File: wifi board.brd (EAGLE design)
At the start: 100 x 80 mm, 28 parts

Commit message: began routing
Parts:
- removed TRANS: RN1906FE, CUSTOM:SOT-563
- removed U$2: CH340G, CUSTOM:SOP-16
- removed U$3: BUTTON, CUSTOM:BUTTON
- removed U$4: TB6593FNG, CUSTOM:SSOP-20
- added C9: 10uF, Seeed-OPL-Capacitor:C0603
- added DRIVER: TB6593FNG, CUSTOM:SSOP-20
- added KEY: PTS645, CUSTOM:BUTTON
- added R10, R9: 10k, resistor:R0603
- added SW: RN1906FE, CUSTOM:SOT-563
- added UART: CH340G, CUSTOM:20-16
- L1: value 10uH -> DFE252012C; device Seeed-OPL-Inductor:L0603 -> CUSTOM:1008
- MDL1: device ESP8266-ESP12E:ESP8266-ESP12E -> adafruit:ESP-12
- R7: value 330k -> 285
- moved C8 225.8 mm to (61.0, 12.1), turned to 180 degrees
- moved U1 221.0 mm to (76.2, 2.54), turned to 90 degrees
- moved D1 219.8 mm to (69.2, 3.81), turned to 90 degrees
- moved C7 216.0 mm to (74.9, 16.5)
- moved R6 214.1 mm to (69.8, 11.4)
- moved R2 211.4 mm to (70.5, 8.89)
- moved C6 207.1 mm to (66.7, 23.5), turned to 90 degrees
- moved R8 206.1 mm to (35.6, 21.0), turned to 270 degrees
- moved R7 201.6 mm to (33.7, 21.0), turned to 90 degrees
- moved C5 198.0 mm to (66.7, 13.3), turned to 90 degrees
- moved CLK 195.7 mm to (67.9, 18.4), turned to 90 degrees
- moved R1 176.1 mm to (51.4, 33.0)
- moved C4 163.9 mm to (59.1, 12.1), turned to 180 degrees
- moved C2 134.6 mm to (35.6, 15.2)
- moved L1 133.7 mm to (34.9, 12.1), turned to 180 degrees
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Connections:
- removed net N$8: OPAMP.4, R7.2
- removed net SLP: REG.8
- new net GP14: MDL1.5
- new net GP15: MDL1.10, R9.2
- new net GP16: MDL1.4
- new net GP2: MDL1.11, R10.2
- new net IN1: DRIVER.18, MDL1.7
- new net IN2: DRIVER.19, MDL1.6
- new net M1: DRIVER.6, DRIVER.7
- new net M2: DRIVER.14, DRIVER.15
- new net PWM: DRIVER.2, MDL1.14
- new net STBY: DRIVER.3, MDL1.13
- net +3V3: now also C9.2, DRIVER.20, L1.P$3, R10.1, REG.8, UART.16, UART.4; no longer L1.2, U$2.16, U$2.4
- net ADC: now also OPAMP.4, R7.2
- net D+: now also UART.5; no longer U$2.5
- net D-: now also UART.6; no longer U$2.6
- net DTR: now also SW.1, SW.5, UART.13; no longer TRANS.1, TRANS.5, U$2.13
- net GND: now also C9.1, DRIVER.1, DRIVER.10, DRIVER.11, DRIVER.12, DRIVER.13, DRIVER.8, DRIVER.9, KEY.3, R9.1, UART.1; no longer U$2.1, U$3.3
- net GP0: now also SW.6; no longer TRANS.6
- net N$1: now also UART.2; no longer U$2.2
- net N$4: now also L1.P$2; no longer L1.1
- net N$7: now also UART.3; no longer U$2.3
- net RST: now also KEY.1, SW.3; no longer TRANS.3
- net RTS: now also SW.2, SW.4, UART.14; no longer TRANS.2, TRANS.4, U$2.14
- net VCC: now also DRIVER.16, DRIVER.17, DRIVER.4, DRIVER.5
- net XI: now also UART.7; no longer U$2.7
- net XO: now also UART.8; no longer U$2.8
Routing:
- net +3V3: track 0.00 -> 100.5 mm, vias 0 -> 7
- net STBY: track 0.00 -> 52.9 mm, vias 0 -> 2
- net PWM: track 0.00 -> 50.3 mm, vias 0 -> 2
- net TX: track 0.00 -> 44.8 mm, vias 0 -> 2
- net VCC: track 0.00 -> 44.4 mm
- net RX: track 0.00 -> 39.7 mm, vias 0 -> 2
- net N$15: track 0.00 -> 29.8 mm, vias 0 -> 2
- net ADC: track 0.00 -> 25.2 mm
- net IN1: track 0.00 -> 18.4 mm
- net N$5: track 0.00 -> 17.2 mm, vias 0 -> 2
- net IN2: track 0.00 -> 15.8 mm
- net N$16: track 0.00 -> 14.9 mm
- net N$17: track 0.00 -> 14.8 mm
- net D-: track 0.00 -> 9.06 mm, vias 0 -> 2
- net N$3: track 0.00 -> 8.67 mm
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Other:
- board size 100 x 80 mm -> 71.1 x 35.6 mm

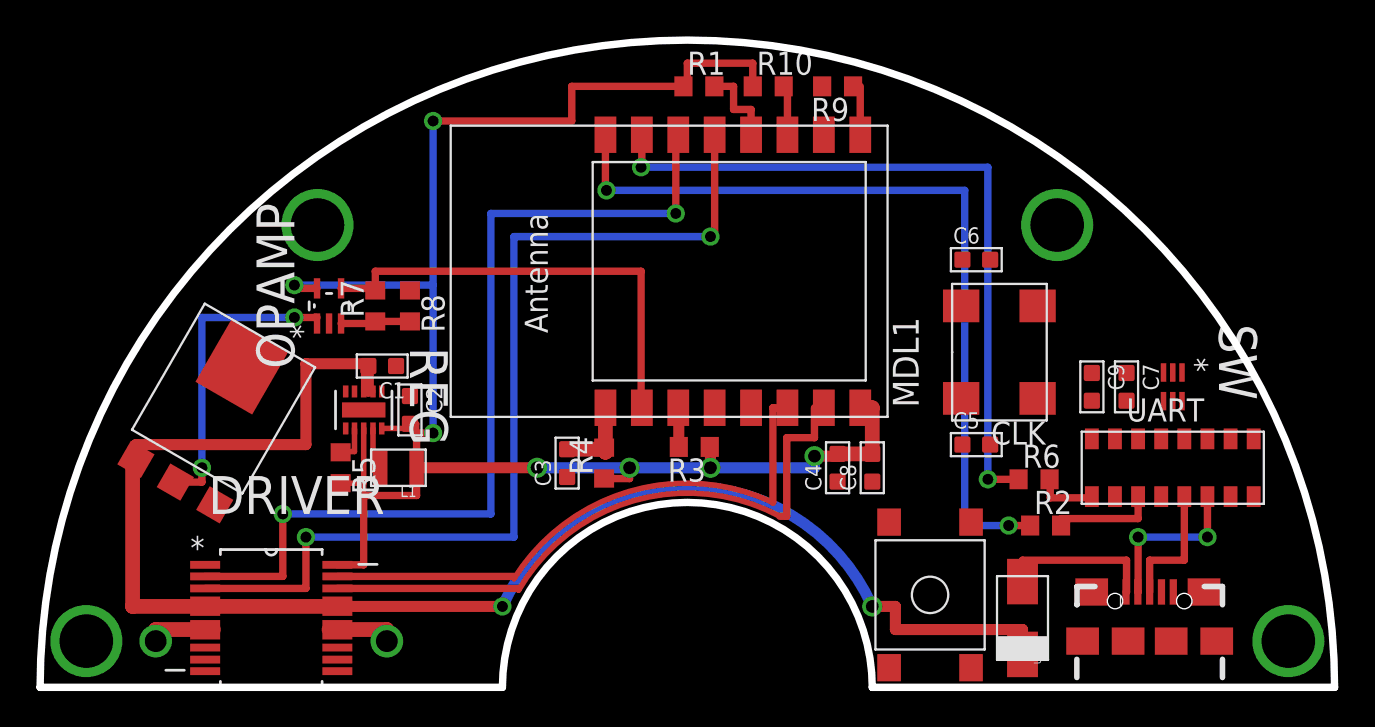
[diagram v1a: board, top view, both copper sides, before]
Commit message: finished routing and made gerber files
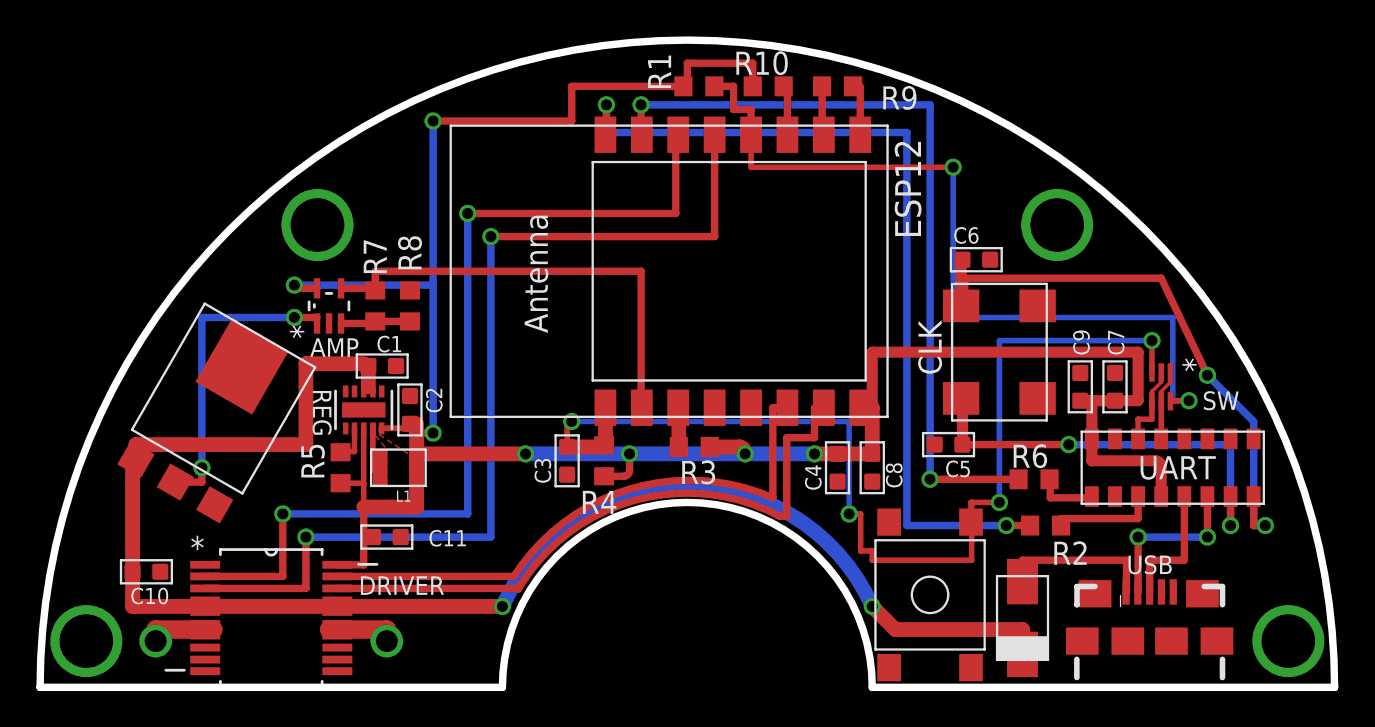
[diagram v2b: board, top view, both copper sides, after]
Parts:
- added C10: 10uF, Seeed-OPL-Capacitor:C0603
- added C11: 100nF, Seeed-OPL-Capacitor:C0603
- moved C5 1.52 mm to (65.2, 13.3), turned to 270 degrees
- moved C7 0.64 mm to (74.3, 16.5)
- moved C9 0.64 mm to (72.4, 16.5)
- moved SW 0.64 mm to (76.8, 16.5)
- moved C3 0.13 mm to (44.2, 12.4)
- moved R4 0.13 mm to (46.2, 12.4)
- renumbered MDL1 to ESP12, OPAMP to AMP, U1 to USB
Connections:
- net N$4 renamed SW
- net +3V3: now also C11.2
- net GND: now also C10.1, C11.1, USB.G1, USB.G2, USB.G3, USB.G4, USB.G5, USB.G6
- net VCC: now also C10.2
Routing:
- net RST: track 4.83 -> 60.2 mm, vias 0 -> 4
- net GP0: track 4.68 -> 44.4 mm, vias 0 -> 2
- net VCC: track 44.4 -> 81.2 mm, vias 0 -> 2
- net +3V3: track 100.5 -> 135.9 mm
- net XO: track 0.00 -> 33.2 mm, vias 0 -> 2
- net N$15: track 29.8 -> 0.00 mm, vias 2 -> 0
- net XI: track 0.00 -> 23.4 mm, vias 0 -> 2
- net N$16: track 14.9 -> 0.00 mm
- net IN1: track 18.4 -> 33.3 mm
- net N$17: track 14.8 -> 0.00 mm
- net IN2: track 15.8 -> 30.4 mm
- net N$8: track 7.62 -> 0.00 mm
- net M2: track 0.00 -> 5.03 mm, vias 0 -> 1
- net M1: track 0.00 -> 5.03 mm, vias 0 -> 1
- net RTS: track 0.00 -> 4.62 mm
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- added copper zone on layer 1, net +3V3
- added copper zone on layer 1, net GND
- added copper zone on layer 16, net GND
- added copper zone on layer 1, net SW

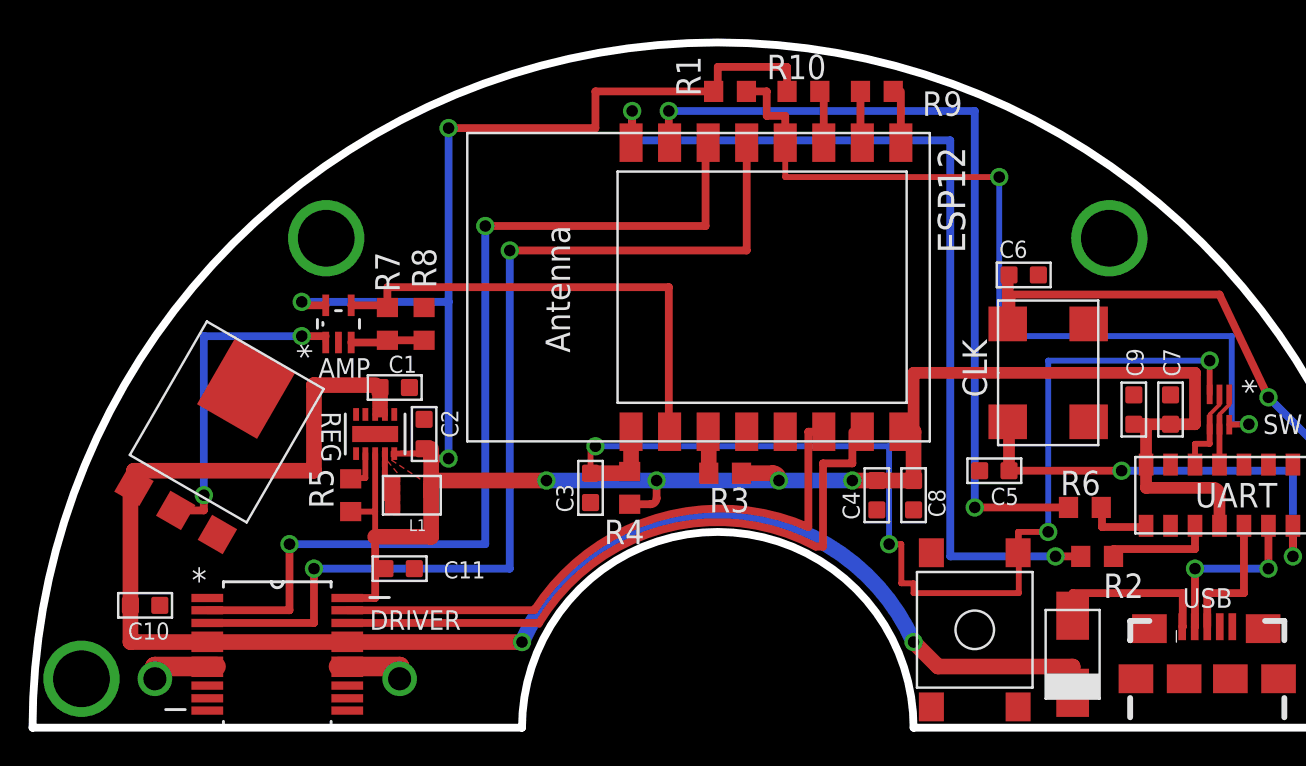
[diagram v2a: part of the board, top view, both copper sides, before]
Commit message: added logo, optimized ground pours
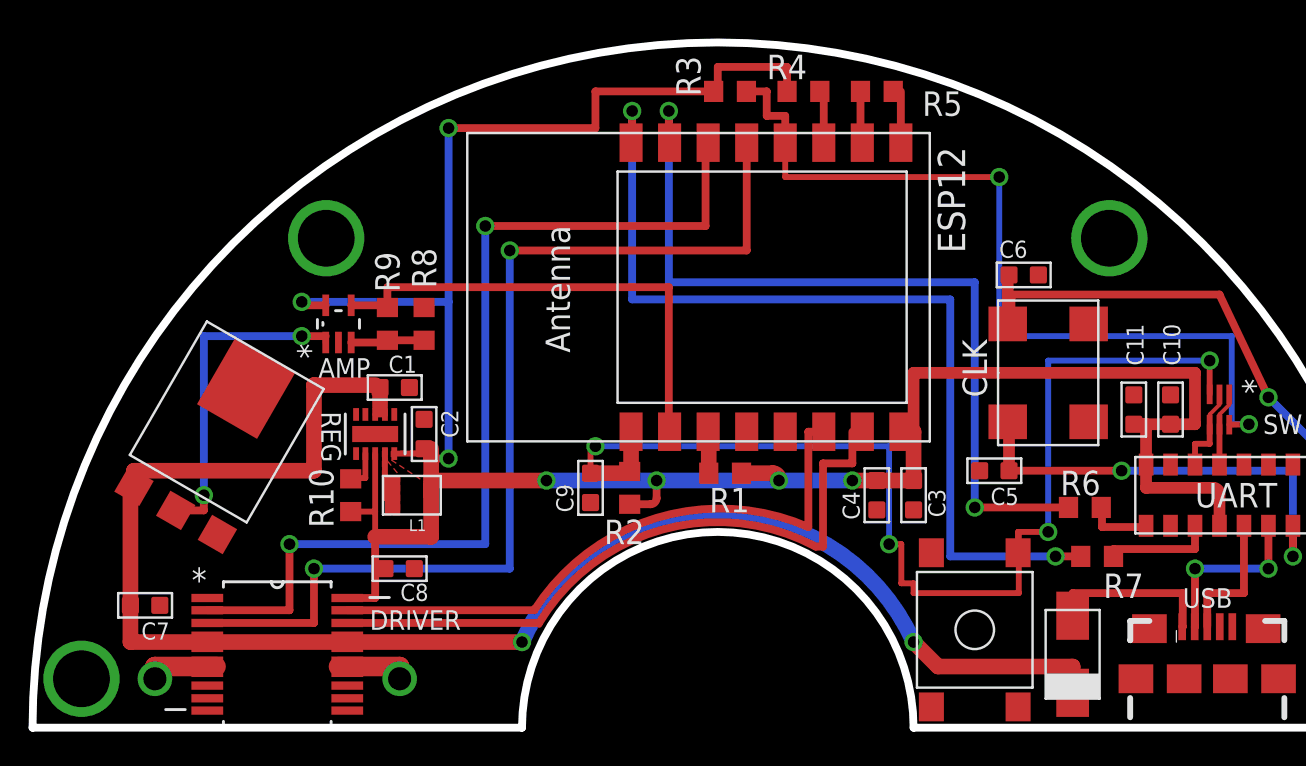
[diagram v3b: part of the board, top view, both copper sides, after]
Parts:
- C10, C8, C9: value 10uF -> 100nF
- C11, C3, C7: value 100nF -> 10uF
- R10: value 10k -> 100k
- R2: value 470 -> 10k
- R5: value 100k -> 10k
- R7: value 285 -> 470
- R9: value 10k -> 285
- moved C10 54.2 mm to (74.3, 16.5), turned to 0 degrees
- moved C7 54.2 mm to (21.1, 6.35), turned to 270 degrees
- moved C11 39.0 mm to (72.4, 16.5), turned to 0 degrees
- moved R7 38.8 mm to (70.5, 8.89), turned to 0 degrees
- moved R5 34.4 mm to (59.1, 33.0), turned to 180 degrees
- moved R10 31.5 mm to (31.8, 12.1), turned to 270 degrees
- moved C9 28.5 mm to (44.2, 12.4), turned to 180 degrees
- moved R9 28.1 mm to (33.7, 21.0), turned to 90 degrees
- moved C8 26.9 mm to (34.3, 8.26), turned to 270 degrees
- moved R2 24.5 mm to (46.2, 12.4), turned to 90 degrees
- moved R4 22.5 mm to (55.2, 33.0), turned to 0 degrees
- moved R1 19.8 mm to (51.2, 13.2), turned to 180 degrees
- moved R3 19.8 mm to (51.4, 33.0), turned to 0 degrees
- moved C3 16.8 mm to (61.0, 12.1)
- renumbered U$1 to CONN
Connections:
- net +3V3: now also C10.2, C3.2, R10.2, R2.1; no longer C7.2, C9.2, R10.1, R5.2
- net ADC: now also R9.2; no longer R7.2
- net EN: now also R1.2; no longer R3.2
- net GND: now also R5.1; no longer R9.1
- net GP0: now also R3.2; no longer R1.2
- net GP15: now also R5.2; no longer R9.2
- net GP2: now also R4.2; no longer R10.2
- net N$1: now also R7.2; no longer R2.2
- net N$2: now also R10.1; no longer R5.1
- net N$6: now also R9.1; no longer R7.1
- net RST: now also C9.2, R2.2; no longer C3.2, R4.2
- net TX: now also R7.1; no longer R2.1
- net VCC: now also C7.2; no longer C10.2
